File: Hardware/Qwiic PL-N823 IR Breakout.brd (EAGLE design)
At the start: 25.4 x 25.4 mm, 39 parts, among them U1 ADS1015, U2 LMV358, U3 PL-N823-01

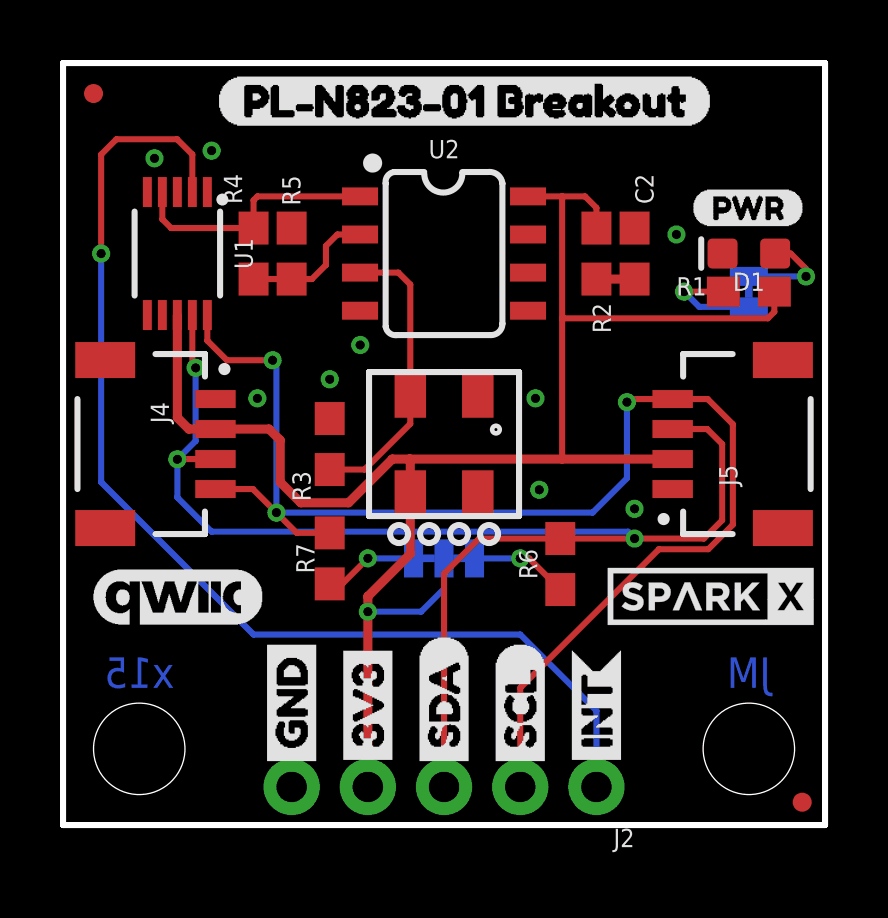
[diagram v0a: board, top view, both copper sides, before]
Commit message: Add no clean note. Change to blue power LED.
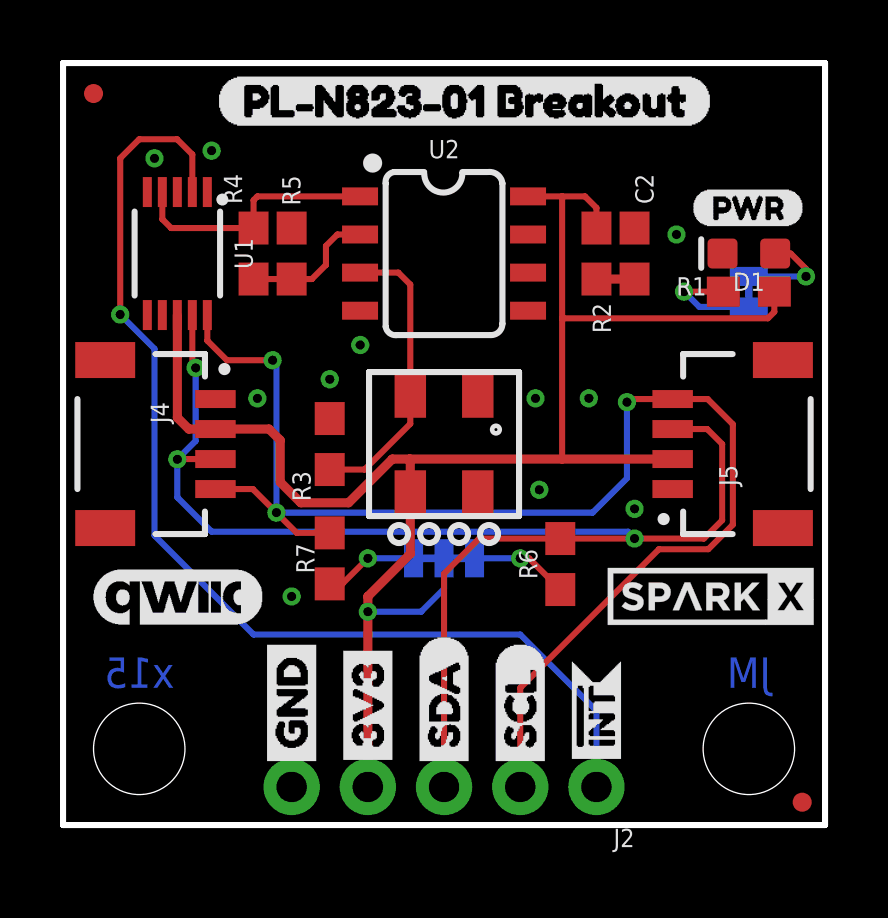
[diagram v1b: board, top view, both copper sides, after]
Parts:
- removed U$21: (no value), buzzard_labels (62):INT0
- added U$11, U$6: (no value), Labels:INT#-[<-04
- D1: value RED -> BLUE
- U$3: device buzzard_labels (62):INT0 -> SparkFun-Aesthetics:PRODUCTION_INSTRUCTIONS
- moved U$3 50.2 mm to (27.9, 50.8), flipped to the top, turned to 0 degrees
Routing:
- net !INT: track 37.8 -> 36.9 mm
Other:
- board text added: "Max reflow temp is 240C"
- board text added: "No clean"
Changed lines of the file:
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@@
 <layer number="44" name="Drills" color="7" fill="1" visible="no" active="yes"/>
 <layer number="45" name="Holes" color="7" fill="1" visible="yes" active="yes"/>
-<layer number="46" name="Milling" color="3" fill="1" visible="yes" active="yes"/>
+<layer number="46" name="Milling" color="3" fill="1" visible="no" active="yes"/>
 <layer number="47" name="Measures" color="7" fill="1" visible="no" active="yes"/>
 <layer number="48" name="Document" color="7" fill="1" visible="no" active="yes"/>
@@
 <text x="2.54" y="5.08" size="1.016" layer="16" font="vector" ratio="15" rot="MR0" align="center">x15</text>
 <text x="22.86" y="5.08" size="1.016" layer="16" font="vector" ratio="15" rot="MR0" align="center">JM</text>
+<text x="29.21" y="38.1" size="1.778" layer="51" font="vector" ratio="15">Max reflow temp is 240C</text>
+<text x="29.21" y="35.56" size="1.778" layer="51" font="vector" ratio="15">No clean</text>
 </plain>
 <attributes>
@@
 <attribute name="VALUE" x="22.86" y="0.889" size="0.6096" layer="27" font="vector" ratio="20" align="top-center"/>
 </element>
-<element name="D1" library="SparkFun-LED" package="LED-0603" value="RED" x="22.86" y="19.05" smashed="yes" rot="R180">
+<element name="D1" library="SparkFun-LED" package="LED-0603" value="BLUE" x="22.86" y="19.05" smashed="yes" rot="R180">
 <attribute name="NAME" x="22.86" y="18.415" size="0.6096" layer="25" font="vector" ratio="20" rot="R180" align="bottom-center"/>
-<attribute name="PROD_ID" value="DIO-00819" x="22.86" y="19.05" size="1.778" layer="27" rot="R180" display="off"/>
-<attribute name="VALUE" value="RED" x="22.86" y="19.685" size="0.6096" layer="27" font="vector" ratio="20" rot="R180" align="top-center"/>
+<attribute name="PROD_ID" value="DIO-08575" x="22.86" y="19.05" size="1.778" layer="27" rot="R180" display="off"/>
+<attribute name="VALUE" value="BLUE" x="22.86" y="19.685" size="0.6096" layer="27" font="vector" ratio="20" rot="R180" align="top-center"/>
 </element>
 <element name="U$1" library="Labels" package="QWIIC_COPYRIGHT_SMALL" value="" x="3.81" y="7.62" smashed="yes"/>
@@
 <attribute name="VALUE" x="19.05" y="3.302" size="0.6096" layer="27" font="vector" ratio="20" rot="R180"/>
 </element>
-<element name="U$21" library="buzzard_labels (62)" package="INT0" value="" x="17.78" y="1.651" smashed="yes" rot="R90"/>
-<element name="U$3" library="buzzard_labels (62)" package="INT0" value="" x="17.78" y="1.651" smashed="yes" rot="MR90"/>
 <element name="U$4" library="buzzard_labels_pln82301" package="PL#N823#01_BREAKOUT0" value="" x="21.59" y="21.59" smashed="yes" rot="MR0"/>
 <element name="U$5" library="Labels" package="I_SUPER2_C-()-03" value="" x="14.097" y="10.668" smashed="yes" rot="MR0"/>
+<element name="U$6" library="Labels" package="INT#-[&lt;-04" value="" x="17.78" y="1.524" smashed="yes" rot="R90"/>
+<element name="U$11" library="Labels" package="INT#-[&lt;-04" value="" x="17.78" y="1.524" smashed="yes" rot="MR90"/>
+<element name="U$3" library="SparkFun-Aesthetics" package="PRODUCTION_INSTRUCTIONS" value="" x="27.94" y="50.8" smashed="yes"/>
 </elements>
 <signals>
@@
 <via x="19.05" y="10.541" extent="1-16" drill="0.3048"/>
 <via x="20.447" y="19.685" extent="1-16" drill="0.3048"/>
+<via x="7.62" y="7.62" extent="1-16" drill="0.3048"/>
+<via x="17.526" y="14.224" extent="1-16" drill="0.3048"/>
 </signal>
 <signal name="N$2">
@@
 <wire x1="4.31" y1="21.1" x2="4.31" y2="22.352" width="0.2032" layer="1"/>
 <wire x1="4.31" y1="22.352" x2="3.802" y2="22.86" width="0.2032" layer="1"/>
-<wire x1="1.778" y1="22.86" x2="1.27" y2="22.352" width="0.2032" layer="1"/>
-<wire x1="1.27" y1="22.352" x2="1.27" y2="19.05" width="0.2032" layer="1"/>
-<via x="1.27" y="19.05" extent="1-16" drill="0.3048"/>
-<wire x1="1.27" y1="19.05" x2="1.27" y2="11.43" width="0.2032" layer="16"/>
+<via x="1.905" y="17.018" extent="1-16" drill="0.3048"/>
+<wire x1="1.905" y1="17.018" x2="3.048" y2="15.875" width="0.2032" layer="16"/>
+<wire x1="3.048" y1="15.875" x2="3.048" y2="9.652" width="0.2032" layer="16"/>
 <wire x1="6.35" y1="6.35" x2="15.24" y2="6.35" width="0.2032" layer="16"/>
 <wire x1="15.24" y1="6.35" x2="17.78" y2="3.81" width="0.2032" layer="16"/>
 <wire x1="17.78" y1="3.81" x2="17.78" y2="1.27" width="0.2032" layer="16"/>
-<wire x1="3.802" y1="22.86" x2="1.778" y2="22.86" width="0.2032" layer="1"/>
-<wire x1="1.27" y1="11.43" x2="6.35" y2="6.35" width="0.2032" layer="16"/>
+<wire x1="3.802" y1="22.86" x2="2.54" y2="22.86" width="0.2032" layer="1"/>
+<wire x1="3.048" y1="9.652" x2="6.35" y2="6.35" width="0.2032" layer="16"/>
+<wire x1="1.905" y1="17.018" x2="1.905" y2="22.225" width="0.2032" layer="1"/>
+<wire x1="1.905" y1="22.225" x2="2.54" y2="22.86" width="0.2032" layer="1"/>
 </signal>
 <signal name="3.3V">

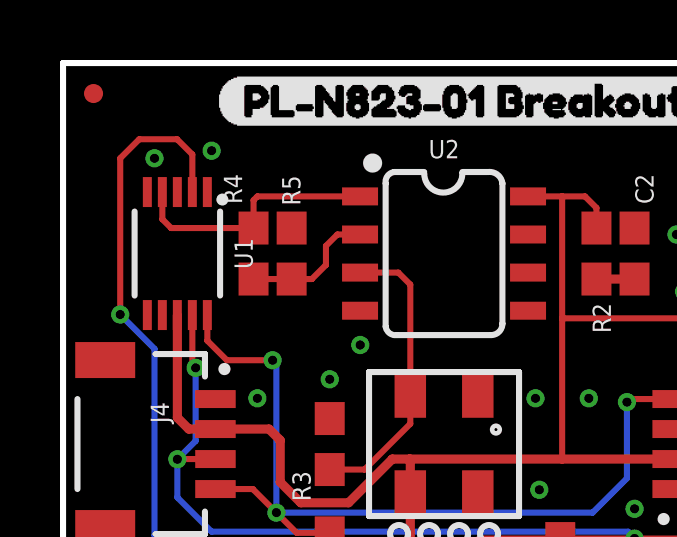
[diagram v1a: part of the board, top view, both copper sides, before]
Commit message: Updated amplifier circuit
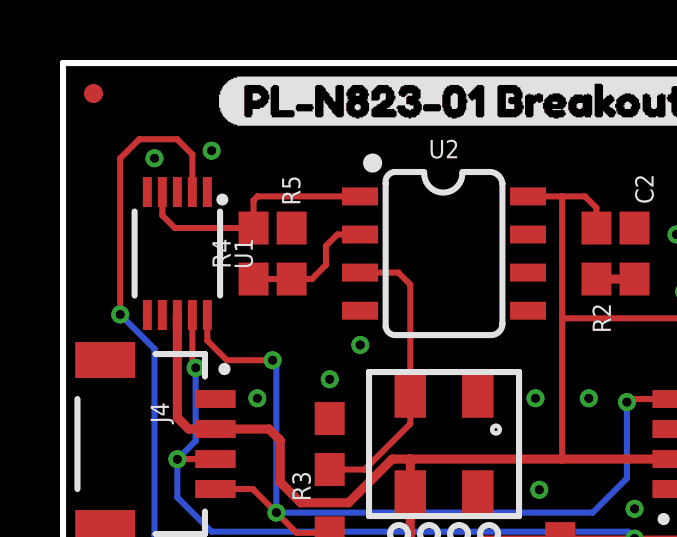
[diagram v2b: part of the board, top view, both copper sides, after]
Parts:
- R4: value 4.7k -> 1.20k
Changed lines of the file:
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@@
 <?xml version="1.0" encoding="utf-8"?>
 <!DOCTYPE eagle SYSTEM "eagle.dtd">
-<eagle version="9.4.0">
+<eagle version="9.4.2">
 <drawing>
 <settings>
@@
 <attribute name="VALUE" value="47k" x="8.255" y="12.1285" size="0.6096" layer="27" ratio="10" rot="R90"/>
 </element>
-<element name="R4" library="SparkFun-Resistors" package="0603" value="4.7k" x="6.35" y="19.05" smashed="yes" rot="R90">
-<attribute name="NAME" x="5.969" y="20.701" size="0.6096" layer="25" rot="R90"/>
-<attribute name="PROD_ID" value="RES-07857" x="6.35" y="19.05" size="1.778" layer="27" rot="R90" display="off"/>
-<attribute name="VALUE" value="4.7k" x="5.7785" y="18.034" size="0.6096" layer="27" rot="R90"/>
-</element>
 <element name="R5" library="SparkFun-Resistors" package="0603" value="1k" x="7.62" y="19.05" smashed="yes" rot="R270">
 <attribute name="NAME" x="7.3025" y="21.6535" size="0.6096" layer="25" rot="R270"/>
@@
 <element name="U$11" library="Labels" package="INT#-[&lt;-04" value="" x="17.78" y="1.524" smashed="yes" rot="MR90"/>
 <element name="U$3" library="SparkFun-Aesthetics" package="PRODUCTION_INSTRUCTIONS" value="" x="27.94" y="50.8" smashed="yes"/>
+<element name="R4" library="SparkFun-Resistors" package="0603" value="1.20k" x="6.35" y="19.05" smashed="yes" rot="R90">
+<attribute name="NAME" x="5.588" y="19.05" size="0.6096" layer="25" font="vector" ratio="20" rot="R90" align="bottom-center"/>
+<attribute name="PROD_ID" value="RES-08413" x="6.35" y="19.05" size="1.778" layer="27" font="vector" ratio="15" rot="R90" display="off"/>
+<attribute name="VALUE" x="7.112" y="19.05" size="0.6096" layer="27" font="vector" ratio="20" rot="R90" align="top-center"/>
+</element>
 </elements>
 <signals>
@@
 <signal name="SIGNAL">
 <contactref element="U2" pad="1"/>
-<contactref element="R4" pad="2"/>
 <contactref element="U1" pad="4"/>
 <wire x1="6.477" y1="20.955" x2="6.35" y2="20.828" width="0.2032" layer="1"/>
+<wire x1="9.9" y1="20.955" x2="6.477" y2="20.955" width="0.2032" layer="1"/>
+<wire x1="3.31" y1="21.1" x2="3.31" y2="20.32" width="0.2032" layer="1"/>
+<contactref element="R4" pad="2"/>
+<wire x1="3.31" y1="20.32" x2="3.73" y2="19.9" width="0.2032" layer="1"/>
+<wire x1="3.73" y1="19.9" x2="6.35" y2="19.9" width="0.2032" layer="1"/>
 <wire x1="6.35" y1="20.828" x2="6.35" y2="19.9" width="0.2032" layer="1"/>
-<wire x1="9.9" y1="20.955" x2="6.477" y2="20.955" width="0.2032" layer="1"/>
-<wire x1="3.603" y1="19.9" x2="6.35" y2="19.9" width="0.2032" layer="1"/>
-<wire x1="3.31" y1="21.1" x2="3.31" y2="20.193" width="0.2032" layer="1"/>
-<wire x1="3.31" y1="20.193" x2="3.603" y2="19.9" width="0.2032" layer="1"/>
 </signal>
 <signal name="SDA">
@@
 <contactref element="U2" pad="2"/>
 <contactref element="R5" pad="2"/>
-<contactref element="R4" pad="1"/>
-<wire x1="7.62" y1="18.2" x2="6.35" y2="18.2" width="0.2032" layer="1"/>
 <wire x1="7.62" y1="18.2" x2="8.294" y2="18.2" width="0.2032" layer="1"/>
 <wire x1="8.763" y1="18.669" x2="8.294" y2="18.2" width="0.2032" layer="1"/>
@@
 <wire x1="9.144" y1="19.685" x2="8.763" y2="19.304" width="0.2032" layer="1"/>
 <wire x1="8.763" y1="19.304" x2="8.763" y2="18.669" width="0.2032" layer="1"/>
+<contactref element="R4" pad="1"/>
+<wire x1="6.35" y1="18.2" x2="7.62" y2="18.2" width="0.2032" layer="1"/>
 </signal>
 <signal name="N$4">
@@
 <mfgpreviewcolor name="substratecolor" color="0xFF786E46"/>
 </mfgpreviewcolors>
-<errors>
-</errors>
 </board>
 </drawing>
